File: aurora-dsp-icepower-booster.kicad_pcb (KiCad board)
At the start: 2 copper layers, 200 x 200 mm, 243 parts, among them J1 XLR_IN_1, J10 XLR3_OUT, J11 XLR3_OUT, J12 XLR3_OUT, J13 24V DC, J14 REMOTE 3.5mm, J2 XLR_IN_2, J3 XLR_IN_3, J4 XLR_IN_4, J5 XLR_IN_5, J6 XLR_IN_6, J7 XLR3_OUT, J8 XLR3_OUT, J9 XLR3_OUT, SW1 Gain CH1, SW2 Gain CH2, SW3 Gain CH3, SW4 Gain CH4, SW5 Gain CH5, SW6 Gain CH6, SW7 ALWAYS/REMOTE, U1 LM4562, U10 LM4562, U11 LM4562, U12 LM4562, U13 TEL5-2422, U14 ADP7118ARDZ-11, U15 ADP7182AUJZ-11, U2 LM4562, U3 LM4562, U4 LM4562, U5 LM4562, U6 LM4562, U7 LM4562, U8 LM4562, U9 LM4562

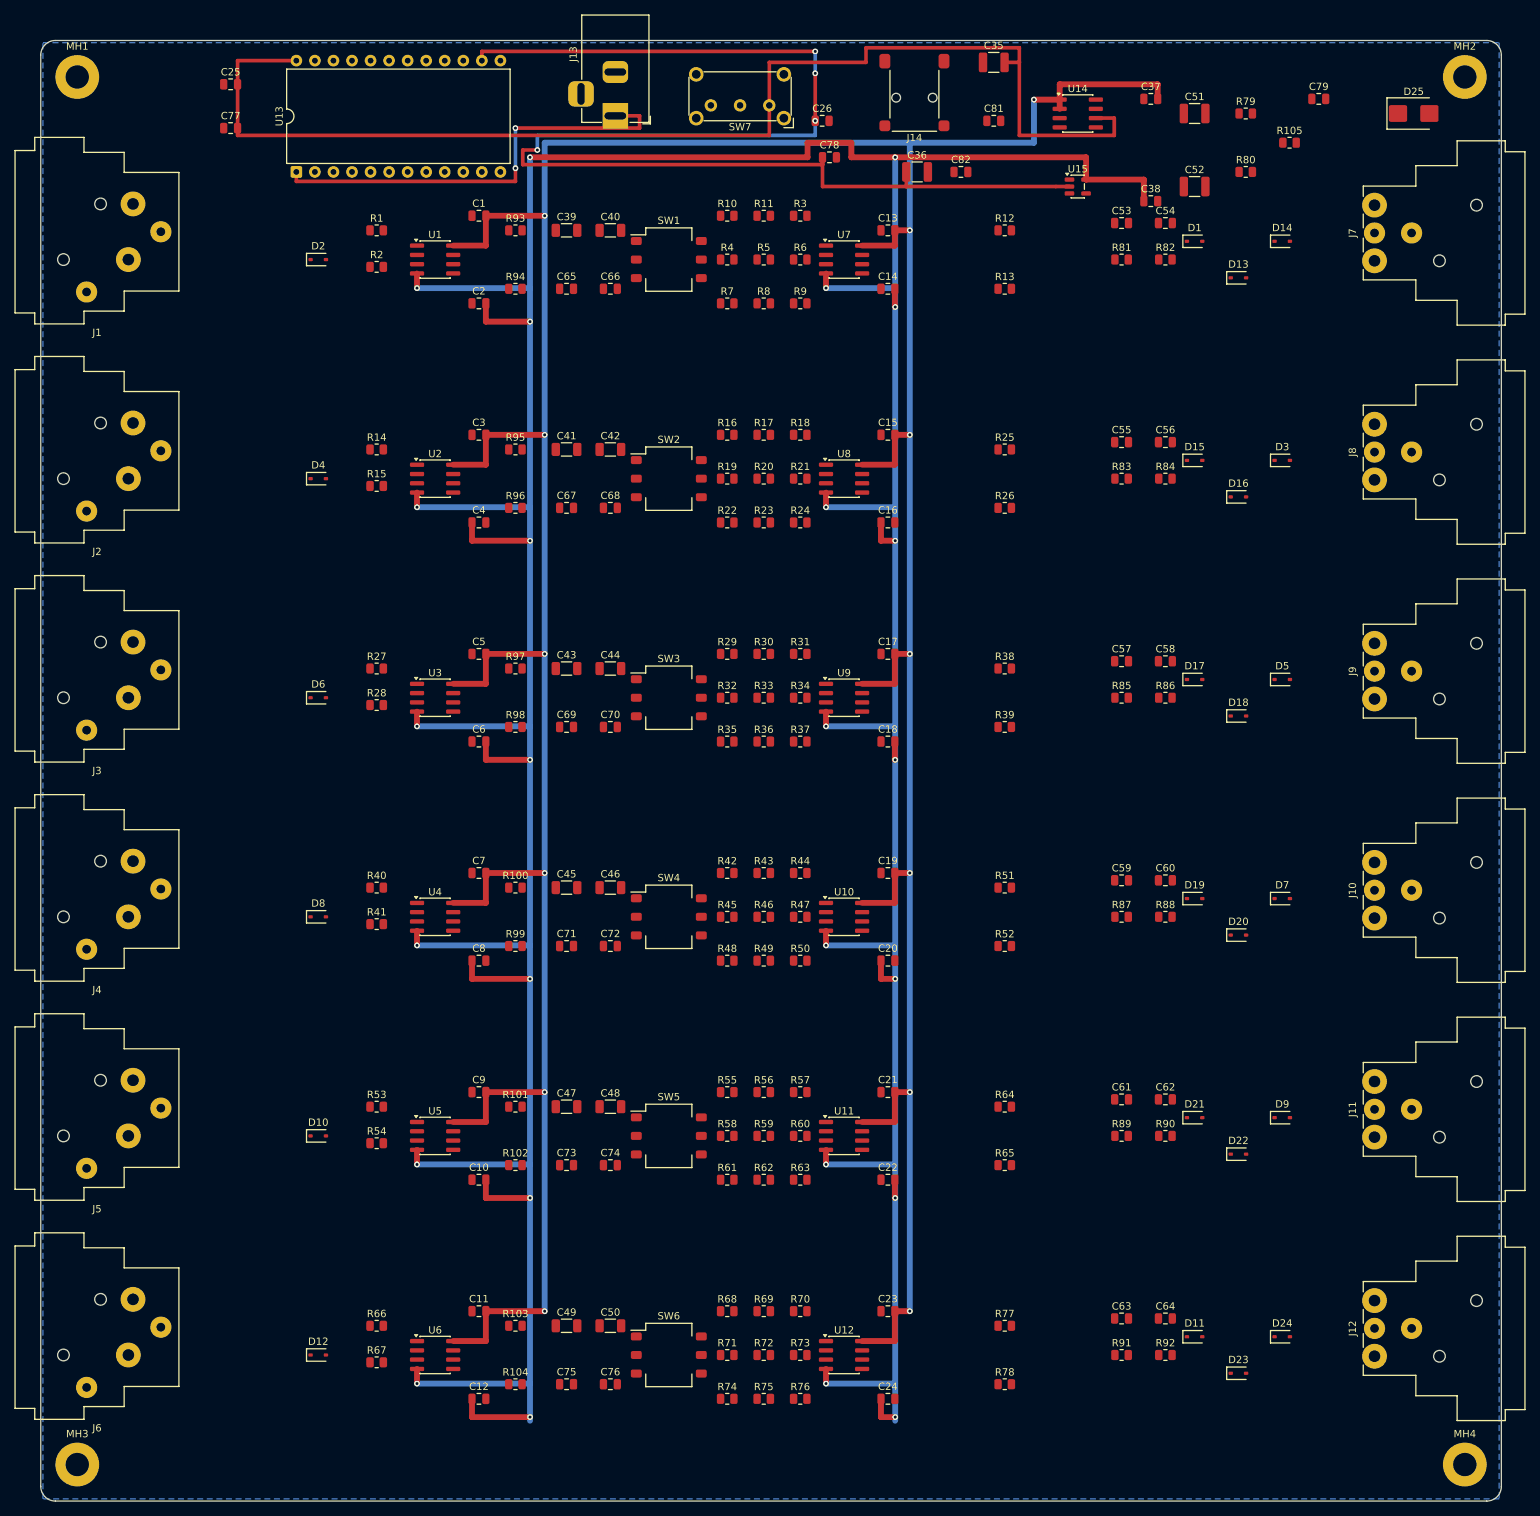
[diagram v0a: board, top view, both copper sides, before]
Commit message: Signal routing v13c: 247 safe stubs, 70 shorts, 32 crossings, 165 signal gaps remaining
- v6 base: pad-avoidance shifting + B.Cu jumpers at crossings
- Two-pass: route all nets first, then fix gaps with safe F.Cu stubs
- Safe stubs: only placed if no pad collision AND no track crossing
- 429 gaps detected, 247 safely fixed, 182 skipped (need manual routing)
- GND unconnected (132) will be fixed by copper pour
- Remaining 165 signal gaps for manual completion in KiCad
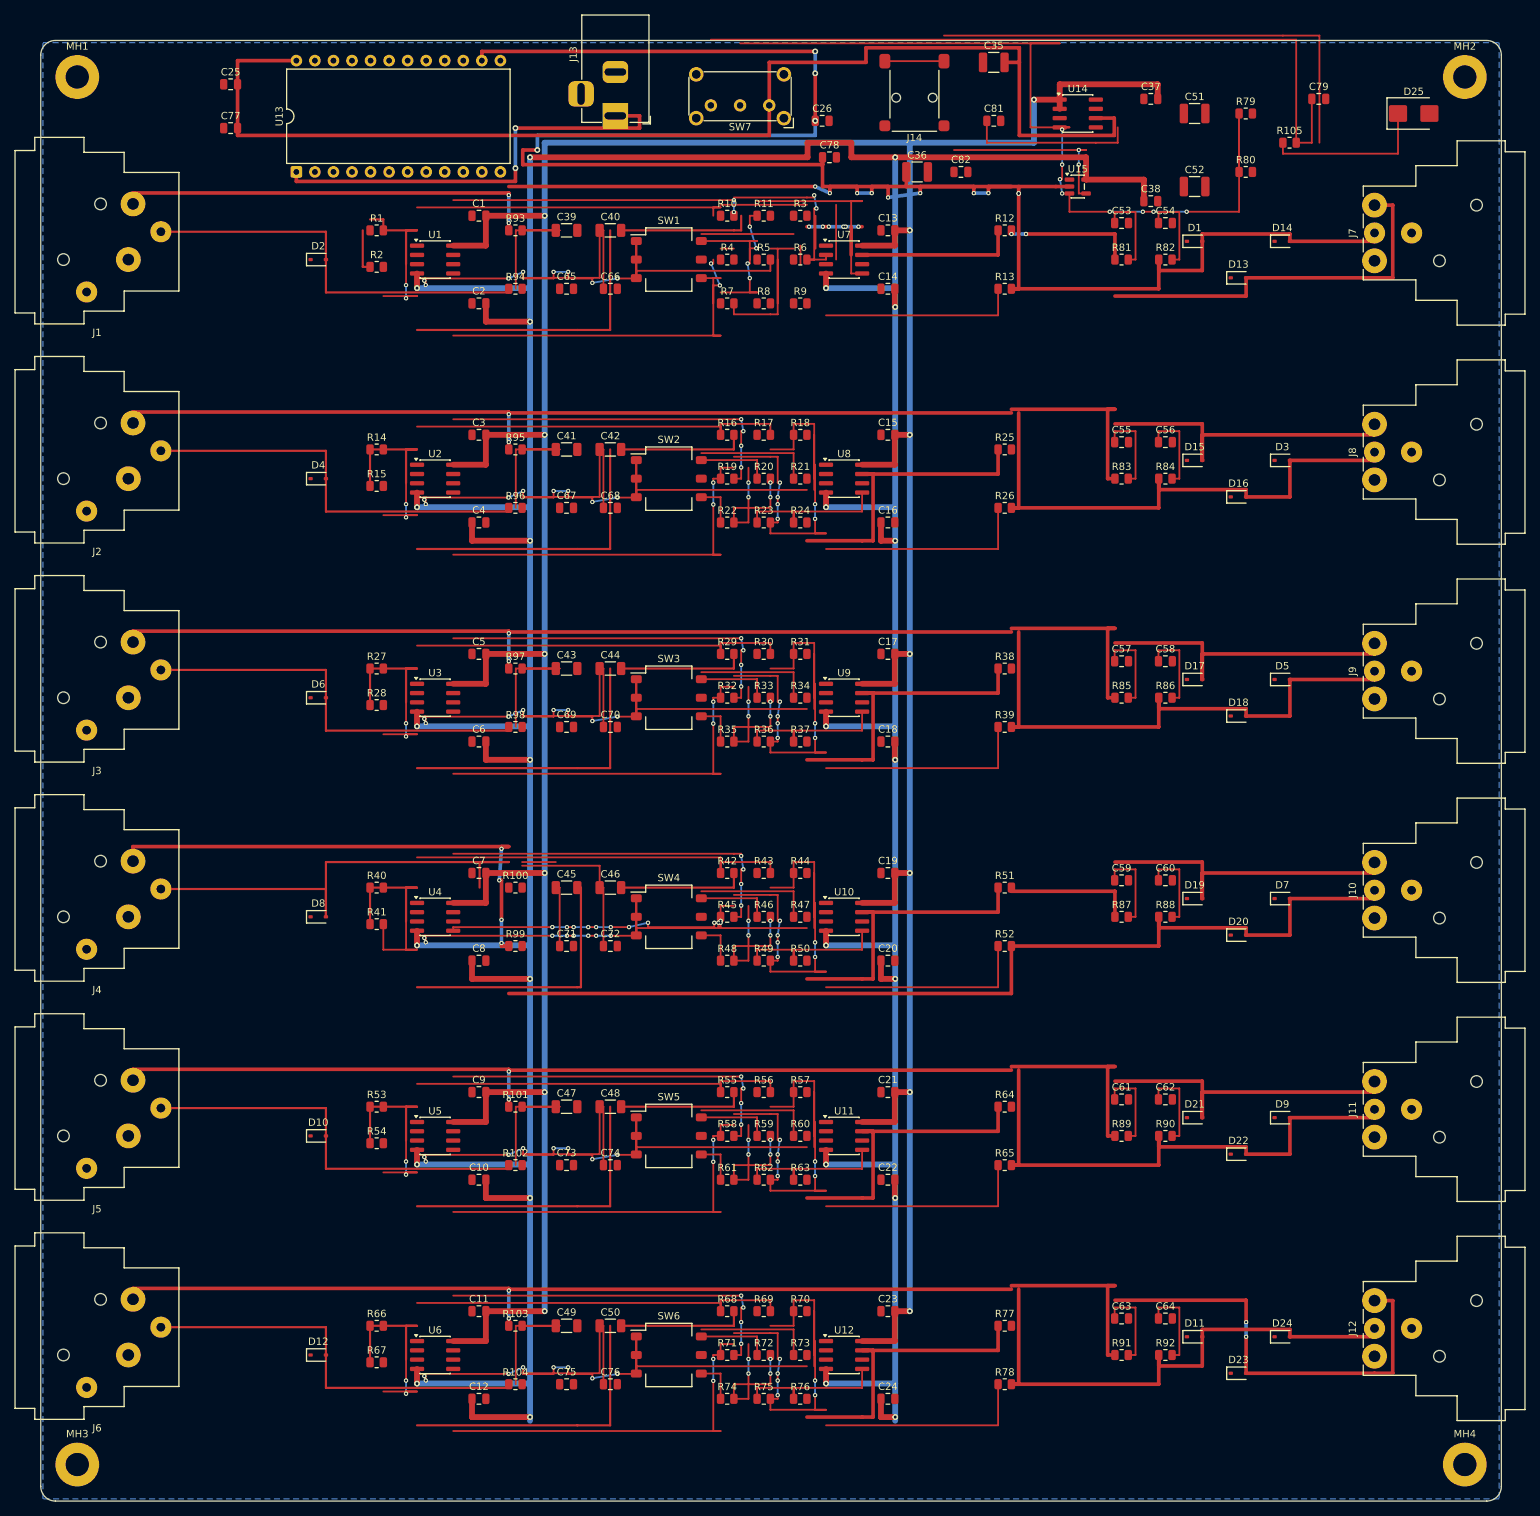
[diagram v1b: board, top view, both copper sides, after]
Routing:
- net /CH1_OUT_COLD: track 0.00 -> 211.4 mm, vias 0 -> 12
- net /CH4_OUT_COLD: track 0.00 -> 207.1 mm, vias 0 -> 4
- net /CH2_OUT_COLD: track 0.00 -> 203.3 mm, vias 0 -> 2
- net /CH6_OUT_COLD: track 0.00 -> 203.3 mm, vias 0 -> 2
- net /CH5_OUT_COLD: track 0.00 -> 203.3 mm, vias 0 -> 2
- net /CH3_OUT_COLD: track 0.00 -> 203.3 mm, vias 0 -> 2
- net /EN_CTRL: track 0.00 -> 123.2 mm, vias 0 -> 8
- net /REMOTE_FILT: track 0.00 -> 102.4 mm
- net /REMOTE_IN: track 0.00 -> 96.9 mm
- net /CH4_RX_OUT: track 0.00 -> 90.2 mm, vias 0 -> 8
- net /CH6_SUMNODE: track 0.00 -> 89.8 mm, vias 0 -> 6
- net /CH5_SUMNODE: track 0.00 -> 89.8 mm, vias 0 -> 6
- net /CH3_SUMNODE: track 0.00 -> 89.8 mm, vias 0 -> 6
- net /CH2_SUMNODE: track 0.00 -> 89.8 mm, vias 0 -> 6
- net /CH6_OUT_HOT: track 0.00 -> 86.2 mm, vias 0 -> 2
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
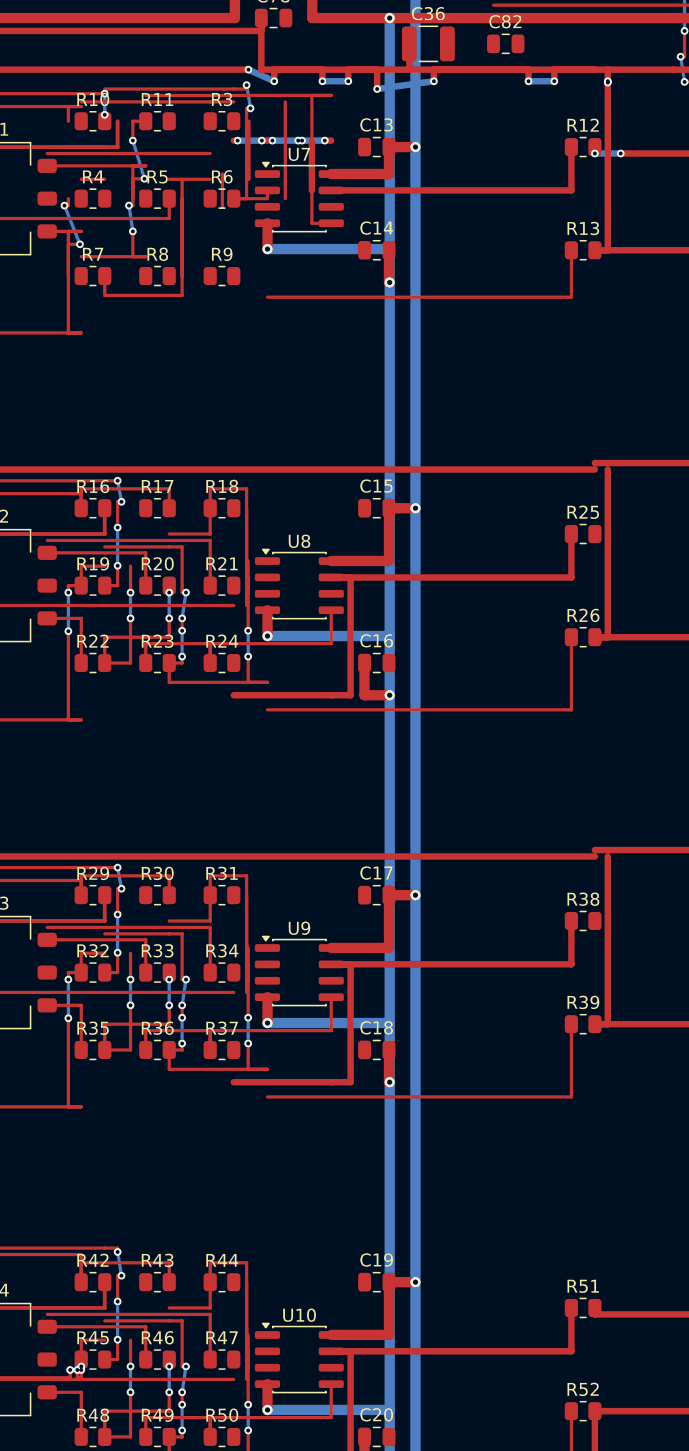
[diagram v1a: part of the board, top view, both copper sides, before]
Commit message: Phase 1: 4 duplicate vias entfernt (hole_to_hole=0)
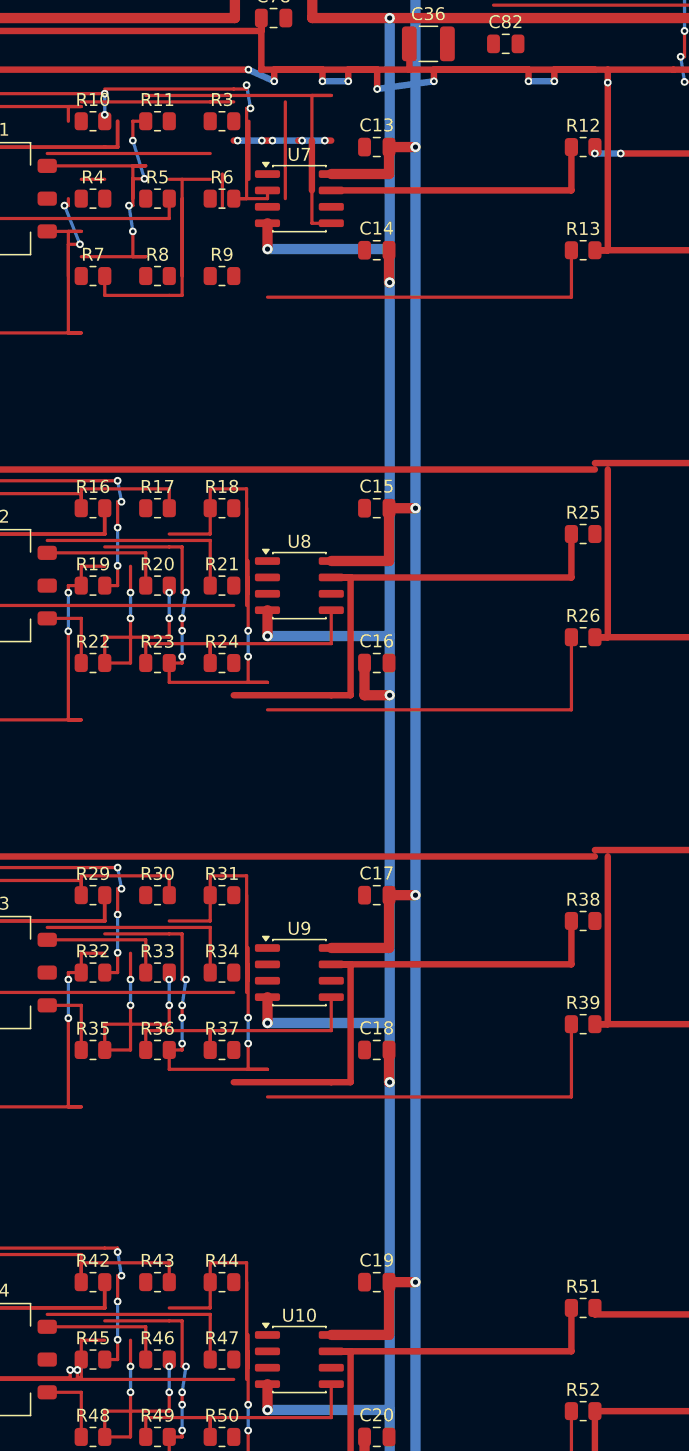
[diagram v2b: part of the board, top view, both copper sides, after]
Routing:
- net /CH4_SUMNODE: vias 16 -> 14
- net /CH1_OUT_DRIVE: vias 6 -> 5
- net /CH1_OUT_COLD: vias 12 -> 11
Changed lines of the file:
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@@
 		(net 13)
 	)
-	(via
-		(at 133.91 20.9)
-		(size 0.6)
-		(drill 0.3)
-		(layers "F.Cu" "B.Cu")
-		(net 13)
-	)
 	(segment
 		(start 116.03 21.5)
@@
 		(net 14)
 	)
-	(via
-		(at 109.91 25.5)
-		(size 0.6)
-		(drill 0.3)
-		(layers "F.Cu" "B.Cu")
-		(net 14)
-	)
 	(segment
 		(start 110.21 25.5)
@@
 	)
 	(via
-		(at 93.09 120.81)
-		(size 0.6)
-		(drill 0.3)
-		(layers "F.Cu" "B.Cu")
-		(net 76)
-	)
-	(via
 		(at 72.97 121.41)
 		(size 0.6)
@@
 		(size 0.6)
 		(drill 0.3)
-		(layers "F.Cu" "B.Cu")
-		(net 76)
-	)
-	(via
-		(at 93.09 120.54)
-		(size 0.6)
-		(drill 0.3)
